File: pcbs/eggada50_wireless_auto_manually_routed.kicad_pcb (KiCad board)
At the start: 2 copper layers, 140.4 x 102.8 mm, 114 parts

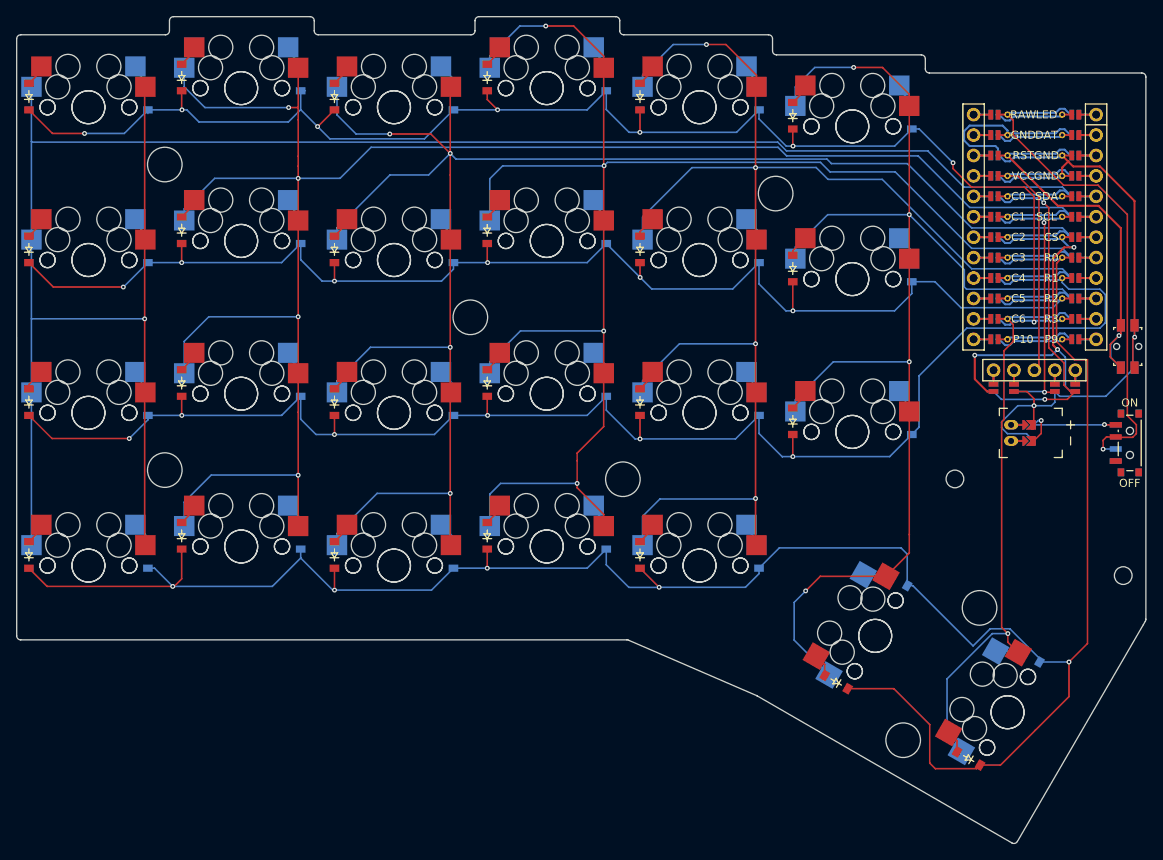
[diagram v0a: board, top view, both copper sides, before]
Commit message: [feat] new manually routed pcb
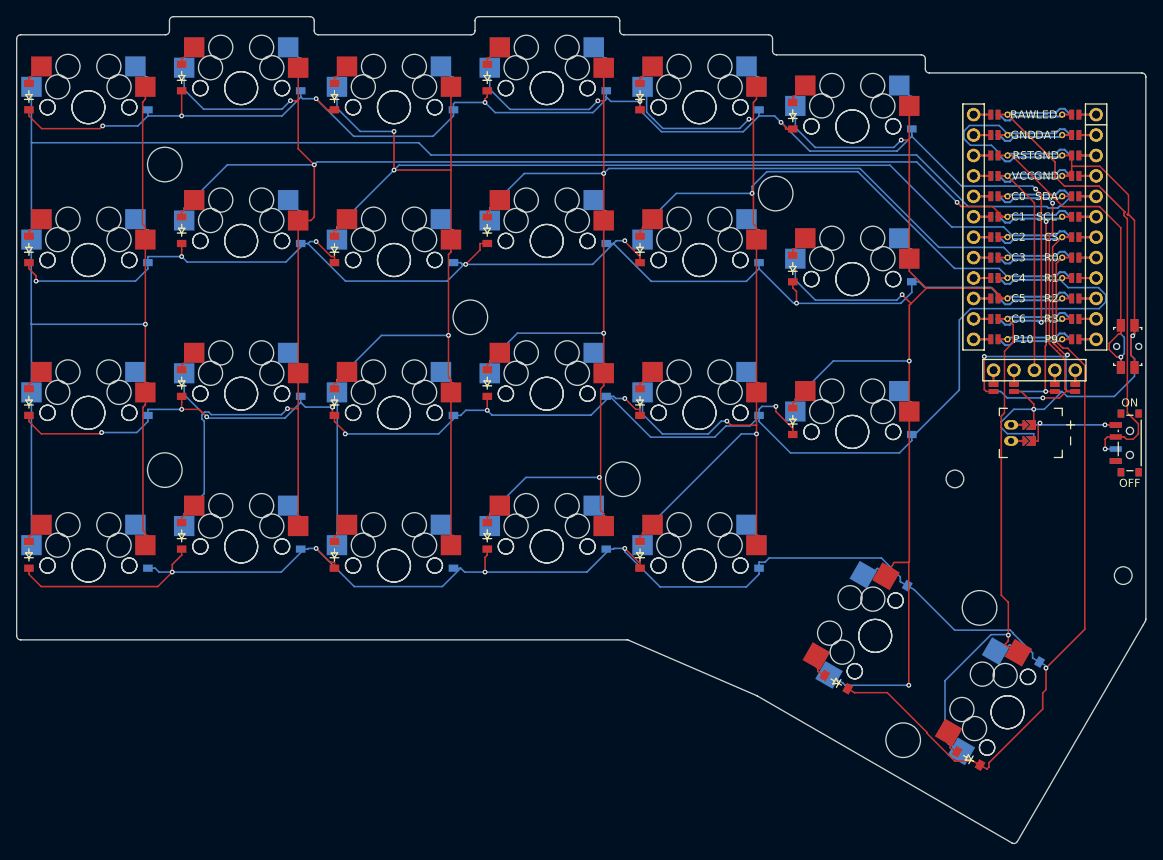
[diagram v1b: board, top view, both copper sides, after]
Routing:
- net C3: track 205.8 -> 193.0 mm
- net C5: track 173.9 -> 162.7 mm
- net R0: track 276.2 -> 265.6 mm
- net C1: track 240.8 -> 230.3 mm
- net C4: track 187.3 -> 180.8 mm
- net R1: track 194.6 -> 198.0 mm, vias 6 -> 8
- net R2: track 172.3 -> 169.1 mm
- net C2: track 222.1 -> 219.1 mm, vias 4 -> 3
- net R3: track 187.5 -> 184.9 mm
- net CS: track 49.6 -> 47.2 mm, vias 3 -> 2
- net C0: track 270.0 -> 271.9 mm
- net C6: track 72.6 -> 74.1 mm
- net SDA: track 47.2 -> 46.1 mm
- net BAT_P: track 15.7 -> 14.7 mm
- net VCC: track 36.4 -> 35.5 mm
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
